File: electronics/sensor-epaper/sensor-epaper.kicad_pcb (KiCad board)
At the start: 4 copper layers, 34 x 79.2 mm, 92 parts, among them J1 i2c, J2 Conn_01x06, J4 Display, J9 USB micro, Q1 Q_NMOS_GSD, Q2 NX2301P, Q3 NX2301P, SW1 SW_Push, U1 ESP32-C3FN4, U2 AMS1117-3.3, U3 NCP1421, Y2 32kHz, Y3 40MHz 10ppm

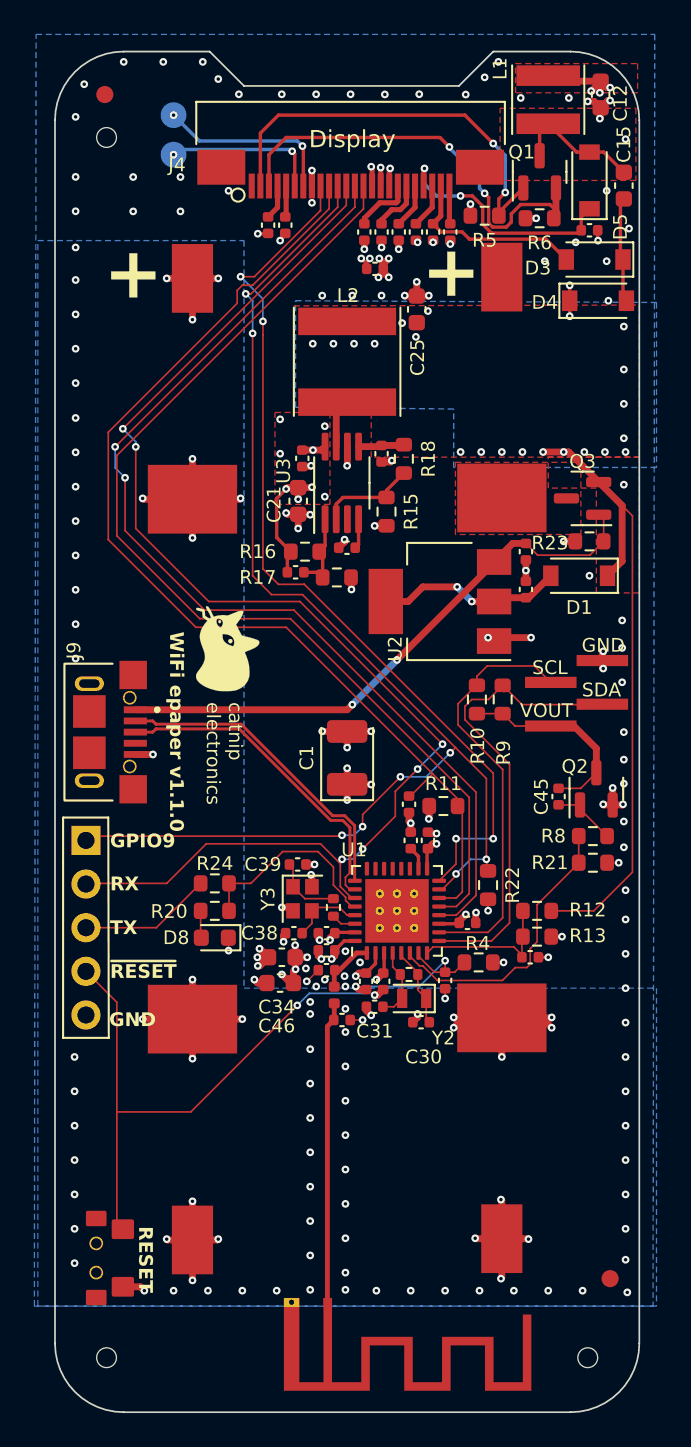
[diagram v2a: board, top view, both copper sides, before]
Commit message: Add cutout in the PCB to decouple SHT40, fix GND connection
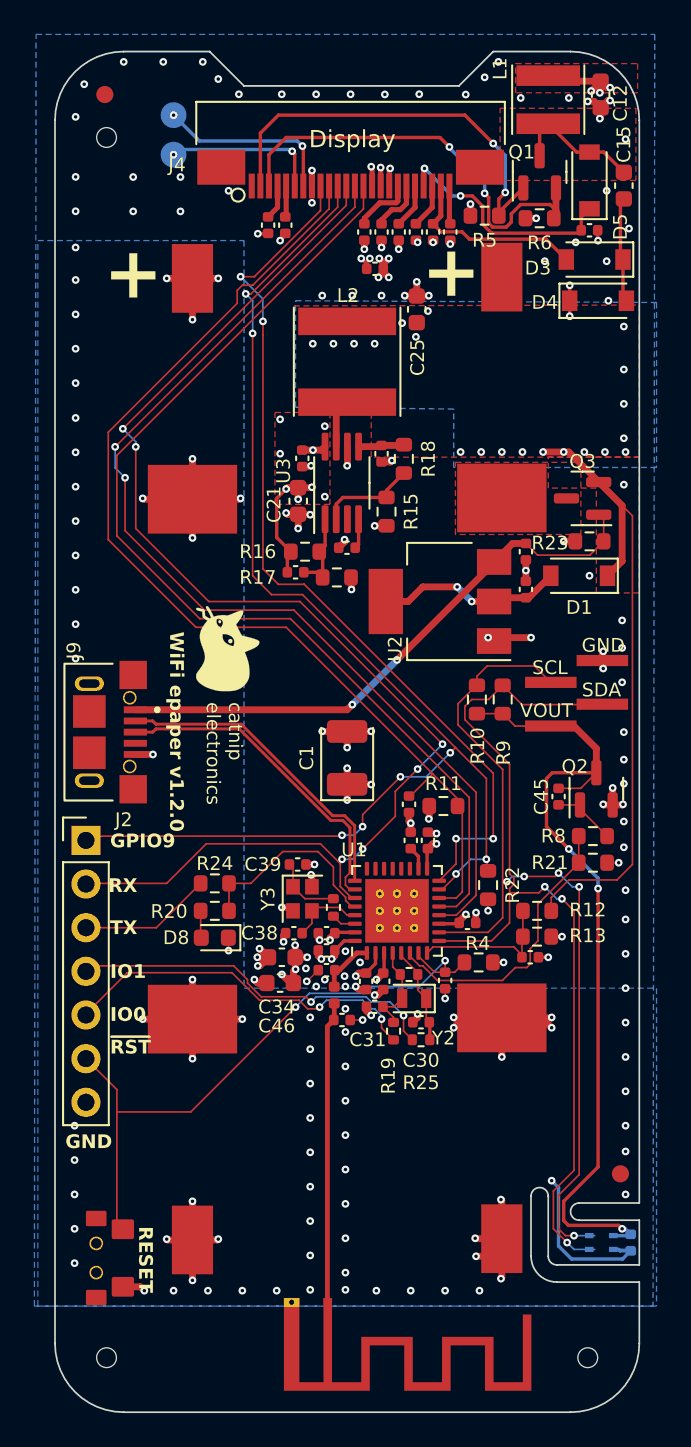
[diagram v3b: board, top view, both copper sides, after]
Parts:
- added C48: 1u, Capacitor_SMD:C_0402_1005Metric, B.Cu at (199.5, 106.3)
- added R19: 0, Resistor_SMD:R_0402_1005Metric, F.Cu at (185.7, 94.0)
- added R25: 0, Resistor_SMD:R_0402_1005Metric, F.Cu at (187.3, 94.5)
- added U4: SHT40-AD1B-R2, miceuz-lib:Sensirion_SHT40-AD1B-R2, B.Cu at (197.8, 106.3)
- J2: footprint Connector_PinHeader_2.54mm:PinHeader_1x05_P2.54mm_Vertical -> Connector_PinHeader_2.54mm:PinHeader_1x07_P2.54mm_Vertical
- moved FID1 6.13 mm to (198.9, 102.3)
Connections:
- J2 pad 4: /CHIP_EN -> /GPIO1
- J2 pad 5: GND -> /GPIO0
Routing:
- net /VI2C: track 11.8 -> 48.7 mm, vias 0 -> 3
- net /I2C_SCL: track 24.6 -> 52.2 mm, vias 0 -> 5
- net /I2C_SDA: track 27.2 -> 53.8 mm, vias 0 -> 3
- net /GPIO1: track 0.00 -> 21.8 mm, vias 0 -> 2
- net /GPIO0: track 0.00 -> 21.4 mm, vias 0 -> 2
- net GND: track 65.9 -> 76.5 mm, vias 194 -> 186
- net /CHIP_EN: track 42.6 -> 37.5 mm
- net /XTAL_32K_P: track 4.04 -> 5.21 mm
- net /XTAL_32K_N: track 4.16 -> 5.19 mm
- net /PREVGH: track 14.4 -> 13.9 mm
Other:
- outline, holes or cut-outs redrawn
- board text added: "IO0"
- board text added: "IO1"
- board text added: "WiFi epaper v1.2.0"
- board text added: "~{RST}"
- board text removed: "WiFi epaper v1.1.0"
- board text removed: "~{RESET}"

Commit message: Add missed electronics files for PCB 1.2.0
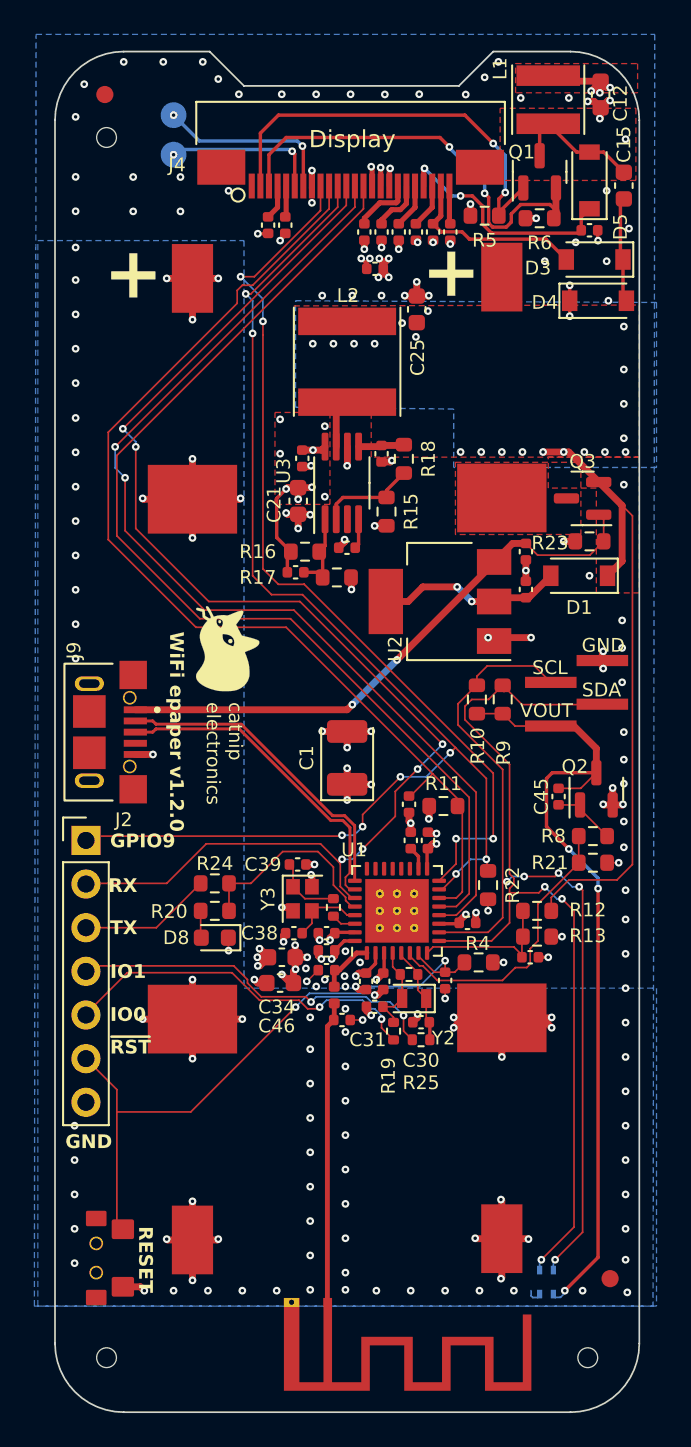
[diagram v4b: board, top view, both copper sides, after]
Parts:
- removed C48: 1u, Capacitor_SMD:C_0402_1005Metric
- C43, C44: value 1u -> 4u7
- moved FID1 6.13 mm to (198.3, 108.4)
- moved U4 3.93 mm to (194.6, 108.6), turned to -90 degrees
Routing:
- net GND: track 76.5 -> 66.9 mm, vias 186 -> 190
- net /VI2C: track 48.7 -> 47.7 mm
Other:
- outline, holes or cut-outs redrawn
